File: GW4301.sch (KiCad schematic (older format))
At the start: 37 parts, among them J1 C64, J2 JTAG, U1 M5LV-PQFP100, U2 DRAM_2Mx8, U3 LD1117S33

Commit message: Fabbed
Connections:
- net VDD is gone; now on net +5V: C10.1, C11.1, C12.1, C13.1, R1.1, R2.1, U2.1 (VDD), U2.14 (VDD)
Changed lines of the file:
@@
 	4800 3700 4700 3700
 Wire Wire Line
-	4700 3700 4700 4000
+	4700 3700 4700 3750
 Wire Wire Line
 	4700 4000 4650 4000
@@
 Wire Wire Line
 	4600 5550 4650 5550
+Wire Wire Line
+	4450 3700 4450 3750
+Wire Wire Line
+	4450 3750 4700 3750
+Connection ~ 4450 3700
+Connection ~ 4700 3750
+Wire Wire Line
+	4700 3750 4700 4000
 $EndSCHEMATC

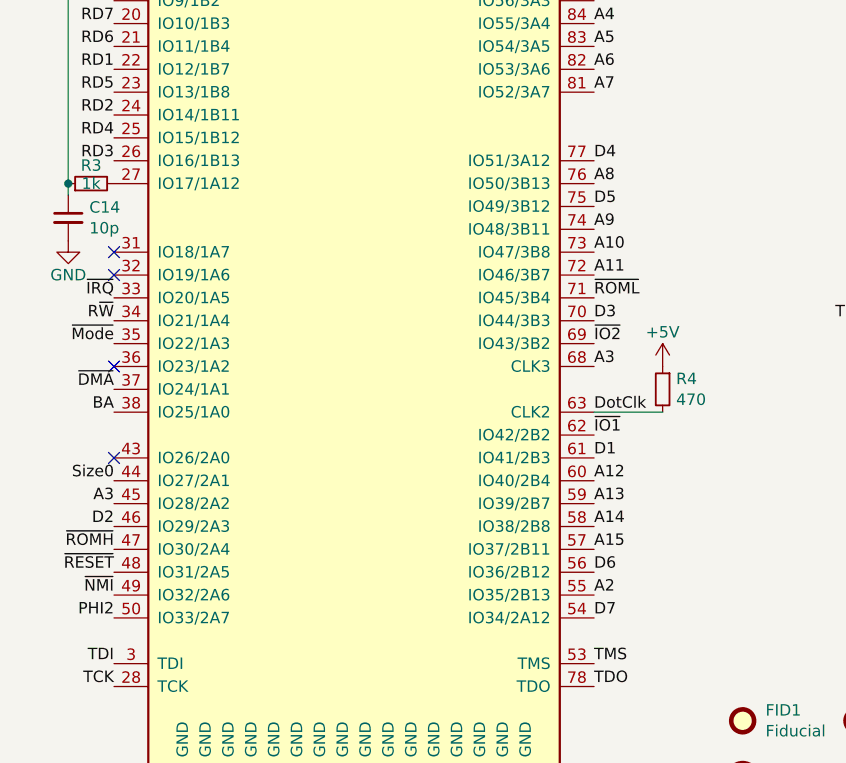
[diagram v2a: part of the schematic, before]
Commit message: Removed extra traces
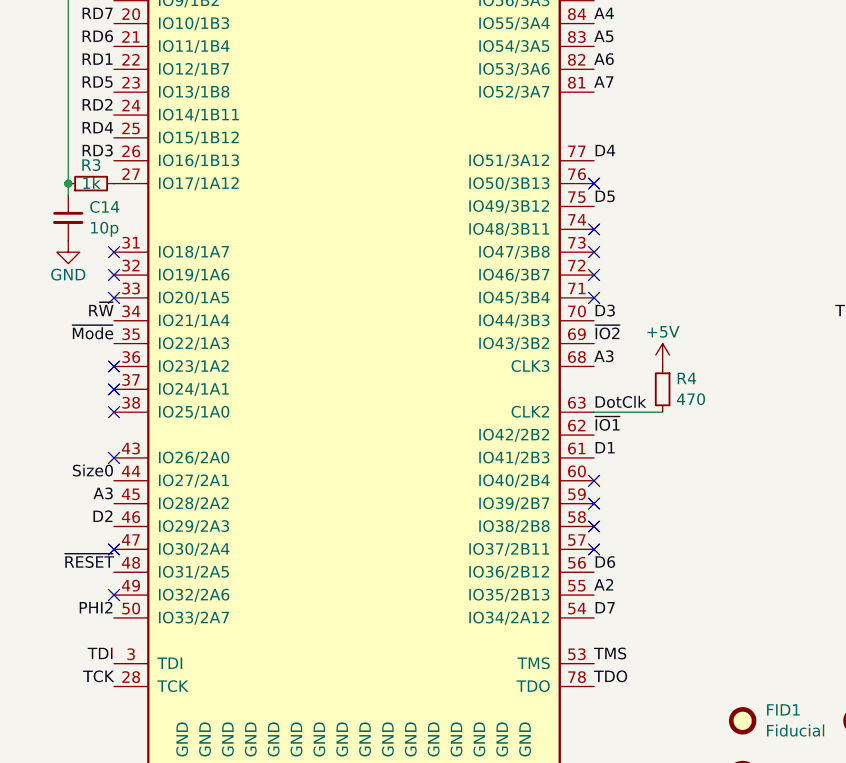
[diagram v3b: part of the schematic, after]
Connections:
- net A10: no longer U1.73 (IO47/3B8)
- net A11: no longer U1.72 (IO46/3B7)
- net A12: no longer U1.60 (IO40/2B4)
- net A13: no longer U1.59 (IO39/2B7)
- net A14: no longer U1.58 (IO38/2B8)
- net A15: no longer U1.57 (IO37/2B11)
- net A8: no longer U1.76 (IO50/3B13)
- net A9: no longer U1.74 (IO48/3B11)
- net BA: no longer U1.38 (IO25/1A0)
- net ~DMA~: no longer U1.37 (IO24/1A1)
- net ~IRQ~: no longer U1.33 (IO20/1A5)
- net ~NMI~: no longer U1.49 (IO32/2A6)
- net ~ROMH~: no longer U1.47 (IO30/2A4)
- net ~ROML~: no longer U1.71 (IO45/3B4)
- no-connect marks 9 -> 23
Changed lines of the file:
@@
 Text Label 3400 5650 0    50   ~ 0
 ~IO2~
-Text Label 1300 5850 2    50   ~ 0
-~DMA~
 Text Label 3400 2950 0    50   ~ 0
 RA0
@@
 Text Label 3400 4150 0    50   ~ 0
 D0
-Text Label 1300 5950 2    50   ~ 0
-BA
-Text Label 3400 5450 0    50   ~ 0
-~ROML~
 $Comp
 L GW_PLD:M5LV-PQFP-100 U1
@@
 Text Label 1300 5550 2    50   ~ 0
 R~W~
-Text Label 1300 5450 2    50   ~ 0
-~IRQ~
 Text Label 3400 3050 0    50   ~ 0
 RA7
@@
 NoConn ~ 1300 5750
 NoConn ~ 1300 6150
-Text Label 1300 6550 2    50   ~ 0
-~ROMH~
 Text Label 1300 6650 2    50   ~ 0
 ~RESET~
-Text Label 1300 6750 2    50   ~ 0
-~NMI~
 Text Label 1300 6850 2    50   ~ 0
 PHI2
-Text Label 3400 6550 0    50   ~ 0
-A15
-Text Label 3400 6450 0    50   ~ 0
-A14
-Text Label 3400 6350 0    50   ~ 0
-A13
-Text Label 3400 6250 0    50   ~ 0
-A12
-Text Label 3400 5350 0    50   ~ 0
-A11
-Text Label 3400 5250 0    50   ~ 0
-A10
 Text Label 3400 4450 0    50   ~ 0
 A6
@@
 Text Label 3400 3850 0    50   ~ 0
 A0
-Text Label 3400 5150 0    50   ~ 0
-A9
-Text Label 3400 4950 0    50   ~ 0
-A8
 Text Label 3400 4550 0    50   ~ 0
 A7
@@
 Wire Wire Line
 	4700 3750 4700 4000
+NoConn ~ 3400 5450
+NoConn ~ 1300 6750
+NoConn ~ 1300 6550
+NoConn ~ 1300 5450
+NoConn ~ 1300 5850
+NoConn ~ 1300 5950
+NoConn ~ 3400 4950
+NoConn ~ 3400 5150
+NoConn ~ 3400 5250
+NoConn ~ 3400 5350
+NoConn ~ 3400 6250
+NoConn ~ 3400 6350
+NoConn ~ 3400 6450
+NoConn ~ 3400 6550
 $EndSCHEMATC
